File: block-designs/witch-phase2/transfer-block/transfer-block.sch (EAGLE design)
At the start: 15 parts, among them IC1 74LVC1G18DBVR, IC2 74AHC1G00DBV, IC3 741G3157DBVR, IC4 741G175, IC5 741G3157DBVR

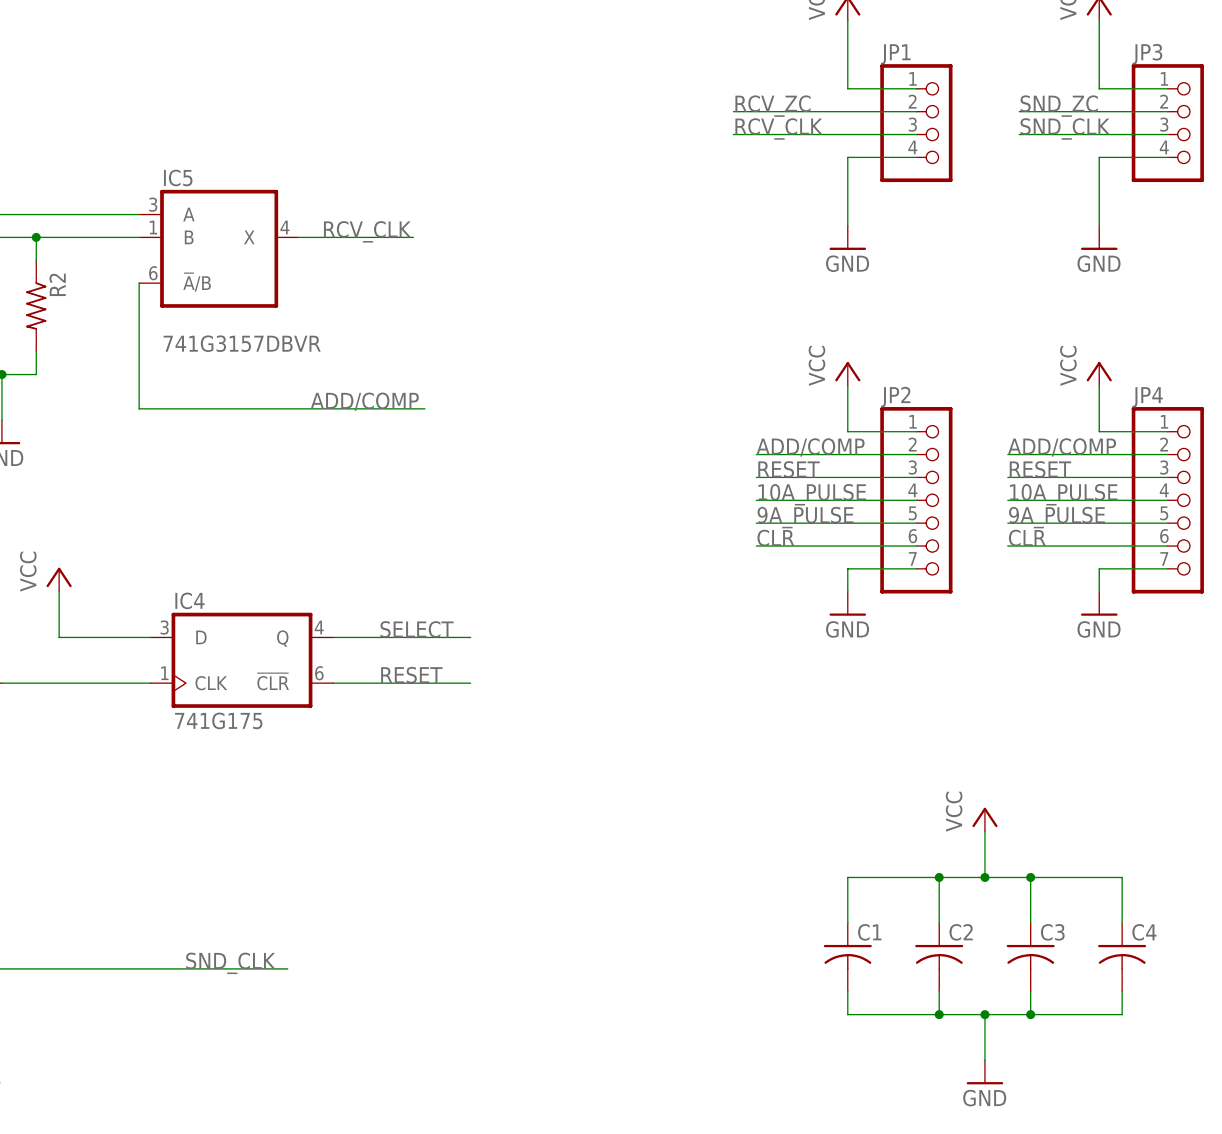
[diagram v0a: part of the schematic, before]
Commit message: updated designs for new labeling and spacing
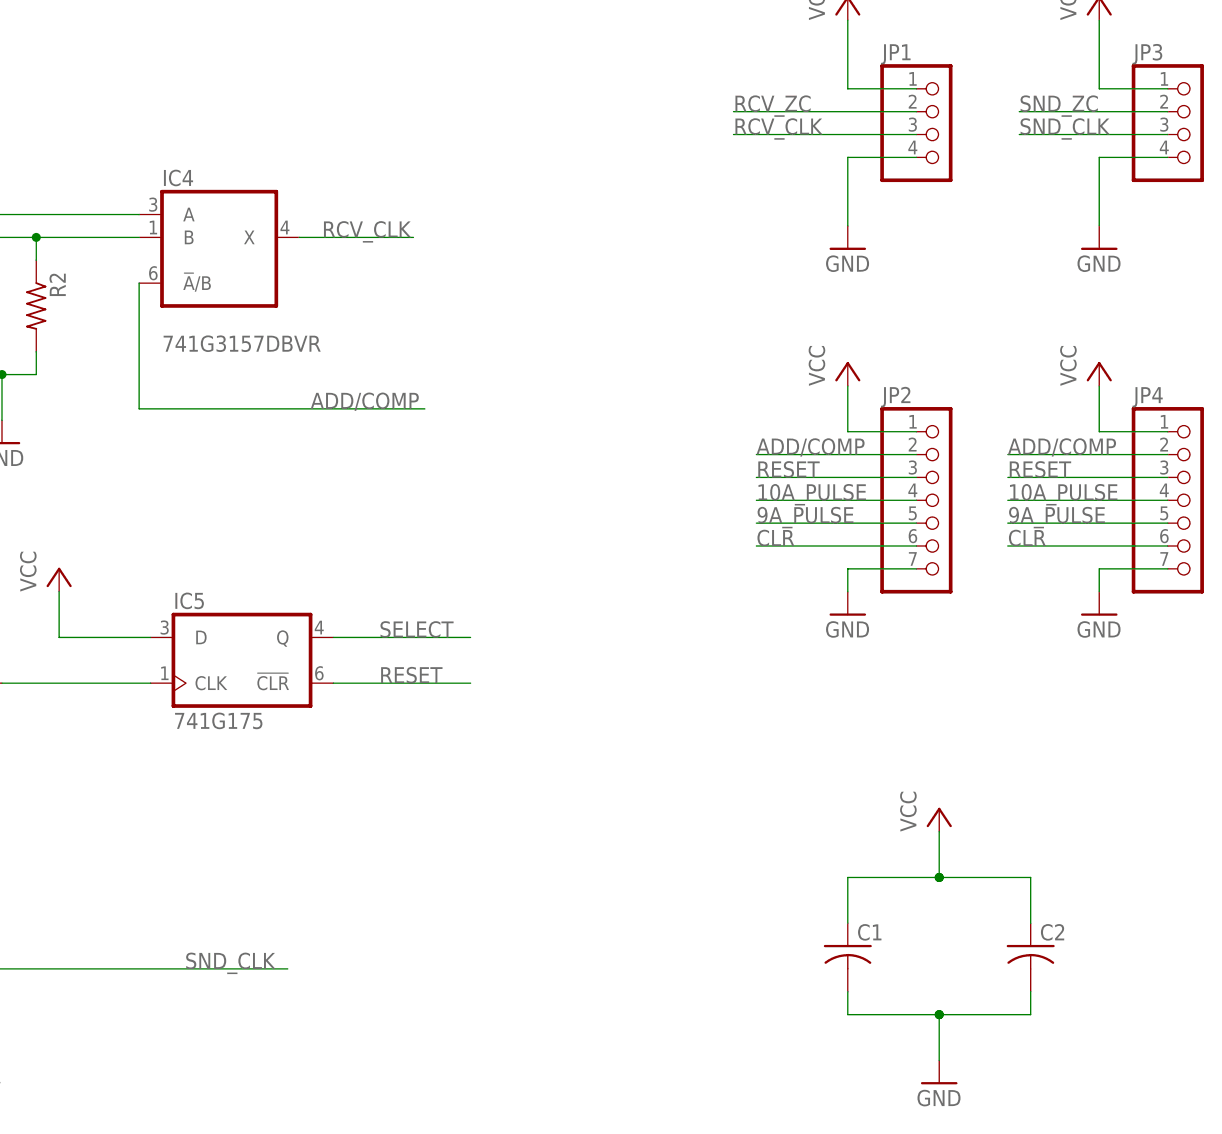
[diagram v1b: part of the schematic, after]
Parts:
- removed C3, C4: (no value), resistor:C-USC0805
- IC4: value 741G175 -> 741G3157DBVR; device 74xx-little-us:741G175 -> 74xx-little-us:741G3157DBVR
- IC5: value 741G3157DBVR -> 741G175; device 74xx-little-us:741G3157DBVR -> 74xx-little-us:741G175
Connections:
- net ADD/COMP: now also IC4G$1.!A!/B; no longer IC5G$1.!A!/B
- net GND: no longer C3.2, C4.2
- net N$4: now also IC4G$1.A; no longer IC5G$1.A
- net N$5: now also IC4G$1.B; no longer IC5G$1.B
- net RCV_CLK: now also IC4G$1.X; no longer IC5G$1.X
- net RESET: now also IC5G$1.!CLR; no longer IC4G$1.!CLR
- net SELECT: now also IC5G$1.Q; no longer IC4G$1.Q
- net VCC: now also IC5G$1.D; no longer C3.1, C4.1, IC4G$1.D
- net ZC_EN: now also IC5G$1.CLK; no longer IC4G$1.CLK
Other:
- moved on the sheet: C2
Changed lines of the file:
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@@
 <setting verticaltext="up"/>
 </settings>
-<grid distance="0.05" unitdist="inch" unit="inch" style="dots" multiple="1" display="no" altdistance="0.01" altunitdist="inch" altunit="inch"/>
+<grid distance="0.1" unitdist="inch" unit="inch" style="dots" multiple="1" display="no" altdistance="0.01" altunitdist="inch" altunit="inch"/>
 <layers>
 <layer number="1" name="Top" color="4" fill="1" visible="no" active="no"/>
@@
 <part name="GND5" library="supply1" deviceset="GND" device=""/>
 <part name="C1" library="resistor" deviceset="C-US" device="C0805"/>
+<part name="GND4" library="supply1" deviceset="GND" device=""/>
 <part name="C2" library="resistor" deviceset="C-US" device="C0805"/>
-<part name="C3" library="resistor" deviceset="C-US" device="C0805"/>
-<part name="GND4" library="supply1" deviceset="GND" device=""/>
-<part name="C4" library="resistor" deviceset="C-US" device="C0805"/>
 <part name="FRAME1" library="frames" deviceset="LETTER_L" device=""/>
 <part name="JP1" library="pinhead" deviceset="PINHD-1X4" device=""/>
@@
 <part name="JP4" library="pinhead" deviceset="PINHD-1X7" device=""/>
 <part name="IC1" library="74xx-little-us" deviceset="74*1G18" device="" value="74LVC1G18DBVR"/>
-<part name="IC5" library="74xx-little-us" deviceset="74*1G3157" device="DBVR"/>
+<part name="IC4" library="74xx-little-us" deviceset="74*1G3157" device="DBVR"/>
 <part name="P+4" library="supply1" deviceset="VCC" device=""/>
 <part name="P+2" library="supply1" deviceset="VCC" device=""/>
@@
 <part name="P+3" library="supply1" deviceset="VCC" device=""/>
 <part name="IC3" library="74xx-little-us" deviceset="74*1G3157" device="DBVR"/>
-<part name="IC4" library="74xx-little-us" deviceset="74*1G175" device=""/>
+<part name="IC5" library="74xx-little-us" deviceset="74*1G175" device=""/>
 </parts>
 <sheets>
@@
 <instance part="GND5" gate="1" x="207.01" y="148.59"/>
 <instance part="C1" gate="G$1" x="179.07" y="71.12"/>
-<instance part="C2" gate="G$1" x="189.23" y="71.12"/>
-<instance part="C3" gate="G$1" x="199.39" y="71.12"/>
-<instance part="GND4" gate="1" x="194.31" y="55.88"/>
-<instance part="C4" gate="G$1" x="209.55" y="71.12"/>
+<instance part="GND4" gate="1" x="189.23" y="55.88"/>
+<instance part="C2" gate="G$1" x="199.39" y="71.12"/>
 <instance part="FRAME1" gate="G$1" x="0" y="0"/>
 <instance part="FRAME1" gate="G$2" x="147.32" y="0"/>
@@
 <instance part="JP4" gate="A" x="217.17" y="120.65"/>
 <instance part="IC1" gate="G$1" x="60.96" y="148.59" rot="MR0"/>
-<instance part="IC5" gate="G$1" x="107.95" y="147.32"/>
-<instance part="P+4" gate="VCC" x="194.31" y="86.36"/>
+<instance part="IC4" gate="G$1" x="107.95" y="147.32"/>
+<instance part="P+4" gate="VCC" x="189.23" y="86.36"/>
 <instance part="P+2" gate="VCC" x="179.07" y="176.53"/>
 <instance part="P+5" gate="VCC" x="207.01" y="176.53"/>
@@
 <instance part="P+3" gate="VCC" x="179.07" y="135.89"/>
 <instance part="IC3" gate="G$1" x="72.39" y="66.04"/>
-<instance part="IC4" gate="G$1" x="109.22" y="102.87"/>
+<instance part="IC5" gate="G$1" x="109.22" y="102.87"/>
 </instances>
 <busses>
@@
 </segment>
 <segment>
-<pinref part="C3" gate="G$1" pin="2"/>
 <wire x1="179.07" y1="63.5" x2="189.23" y2="63.5" width="0.1524" layer="91"/>
-<wire x1="189.23" y1="63.5" x2="194.31" y2="63.5" width="0.1524" layer="91"/>
-<wire x1="194.31" y1="63.5" x2="199.39" y2="63.5" width="0.1524" layer="91"/>
-<wire x1="199.39" y1="63.5" x2="199.39" y2="66.04" width="0.1524" layer="91"/>
 <pinref part="C1" gate="G$1" pin="2"/>
 <wire x1="179.07" y1="66.04" x2="179.07" y2="63.5" width="0.1524" layer="91"/>
 <pinref part="C2" gate="G$1" pin="2"/>
-<wire x1="189.23" y1="66.04" x2="189.23" y2="63.5" width="0.1524" layer="91"/>
-<pinref part="C4" gate="G$1" pin="2"/>
-<wire x1="209.55" y1="66.04" x2="209.55" y2="63.5" width="0.1524" layer="91"/>
-<wire x1="209.55" y1="63.5" x2="199.39" y2="63.5" width="0.1524" layer="91"/>
-<junction x="199.39" y="63.5"/>
+<wire x1="199.39" y1="66.04" x2="199.39" y2="63.5" width="0.1524" layer="91"/>
+<wire x1="199.39" y1="63.5" x2="189.23" y2="63.5" width="0.1524" layer="91"/>
 <junction x="189.23" y="63.5"/>
 <pinref part="GND4" gate="1" pin="GND"/>
-<wire x1="194.31" y1="58.42" x2="194.31" y2="63.5" width="0.1524" layer="91"/>
-<junction x="194.31" y="63.5"/>
+<wire x1="189.23" y1="58.42" x2="189.23" y2="63.5" width="0.1524" layer="91"/>
+<junction x="189.23" y="63.5"/>
 </segment>
 <segment>
@@
 <segment>
 <pinref part="IC1" gate="G$1" pin="Y1"/>
-<pinref part="IC5" gate="G$1" pin="A"/>
+<pinref part="IC4" gate="G$1" pin="A"/>
 <wire x1="69.85" y1="152.4" x2="81.28" y2="152.4" width="0.1524" layer="91"/>
 <pinref part="R1" gate="G$1" pin="1"/>
@@
 <segment>
 <pinref part="IC1" gate="G$1" pin="Y0"/>
-<pinref part="IC5" gate="G$1" pin="B"/>
+<pinref part="IC4" gate="G$1" pin="B"/>
 <wire x1="69.85" y1="149.86" x2="88.9" y2="149.86" width="0.1524" layer="91"/>
 <pinref part="R2" gate="G$1" pin="1"/>
@@
 <net name="VCC" class="0">
 <segment>
-<pinref part="C3" gate="G$1" pin="1"/>
 <wire x1="179.07" y1="78.74" x2="189.23" y2="78.74" width="0.1524" layer="91"/>
-<wire x1="189.23" y1="78.74" x2="194.31" y2="78.74" width="0.1524" layer="91"/>
-<wire x1="194.31" y1="78.74" x2="199.39" y2="78.74" width="0.1524" layer="91"/>
-<wire x1="199.39" y1="78.74" x2="199.39" y2="73.66" width="0.1524" layer="91"/>
 <pinref part="C1" gate="G$1" pin="1"/>
 <wire x1="179.07" y1="73.66" x2="179.07" y2="78.74" width="0.1524" layer="91"/>
 <pinref part="C2" gate="G$1" pin="1"/>
-<wire x1="189.23" y1="73.66" x2="189.23" y2="78.74" width="0.1524" layer="91"/>
-<pinref part="C4" gate="G$1" pin="1"/>
-<wire x1="199.39" y1="78.74" x2="209.55" y2="78.74" width="0.1524" layer="91"/>
-<wire x1="209.55" y1="78.74" x2="209.55" y2="73.66" width="0.1524" layer="91"/>
+<wire x1="189.23" y1="78.74" x2="199.39" y2="78.74" width="0.1524" layer="91"/>
+<wire x1="199.39" y1="78.74" x2="199.39" y2="73.66" width="0.1524" layer="91"/>
 <junction x="189.23" y="78.74"/>
-<junction x="199.39" y="78.74"/>
-<wire x1="194.31" y1="78.74" x2="194.31" y2="83.82" width="0.1524" layer="91"/>
-<junction x="194.31" y="78.74"/>
+<wire x1="189.23" y1="78.74" x2="189.23" y2="83.82" width="0.1524" layer="91"/>
+<junction x="189.23" y="78.74"/>
 <pinref part="P+4" gate="VCC" pin="VCC"/>
 </segment>
@@
 <wire x1="91.44" y1="105.41" x2="91.44" y2="110.49" width="0.1524" layer="91"/>
 <pinref part="P+1" gate="VCC" pin="VCC"/>
-<pinref part="IC4" gate="G$1" pin="D"/>
+<pinref part="IC5" gate="G$1" pin="D"/>
 </segment>
 <segment>
@@
 <net name="ADD/COMP" class="0">
 <segment>
-<pinref part="IC5" gate="G$1" pin="!A!/B"/>
+<pinref part="IC4" gate="G$1" pin="!A!/B"/>
 <wire x1="100.33" y1="144.78" x2="100.33" y2="130.81" width="0.1524" layer="91"/>
 <wire x1="100.33" y1="130.81" x2="132.08" y2="130.81" width="0.1524" layer="91"/>
@@
 </segment>
 <segment>
-<pinref part="IC4" gate="G$1" pin="Q"/>
+<pinref part="IC5" gate="G$1" pin="Q"/>
 <wire x1="121.92" y1="105.41" x2="137.16" y2="105.41" width="0.1524" layer="91"/>
 <label x="127" y="105.41" size="1.778" layer="95"/>
@@
 <pinref part="IC2" gate="A" pin="O"/>
 <wire x1="85.09" y1="100.33" x2="101.6" y2="100.33" width="0.1524" layer="91"/>
-<pinref part="IC4" gate="G$1" pin="CLK"/>
+<pinref part="IC5" gate="G$1" pin="CLK"/>
 </segment>
 </net>
@@
 </segment>
 <segment>
-<pinref part="IC5" gate="G$1" pin="X"/>
+<pinref part="IC4" gate="G$1" pin="X"/>
 <wire x1="118.11" y1="149.86" x2="130.81" y2="149.86" width="0.1524" layer="91"/>
 <label x="120.65" y="149.86" size="1.778" layer="95"/>
@@
 </segment>
 <segment>
-<pinref part="IC4" gate="G$1" pin="!CLR"/>
+<pinref part="IC5" gate="G$1" pin="!CLR"/>
 <wire x1="121.92" y1="100.33" x2="137.16" y2="100.33" width="0.1524" layer="91"/>
 <label x="127" y="100.33" size="1.778" layer="95"/>

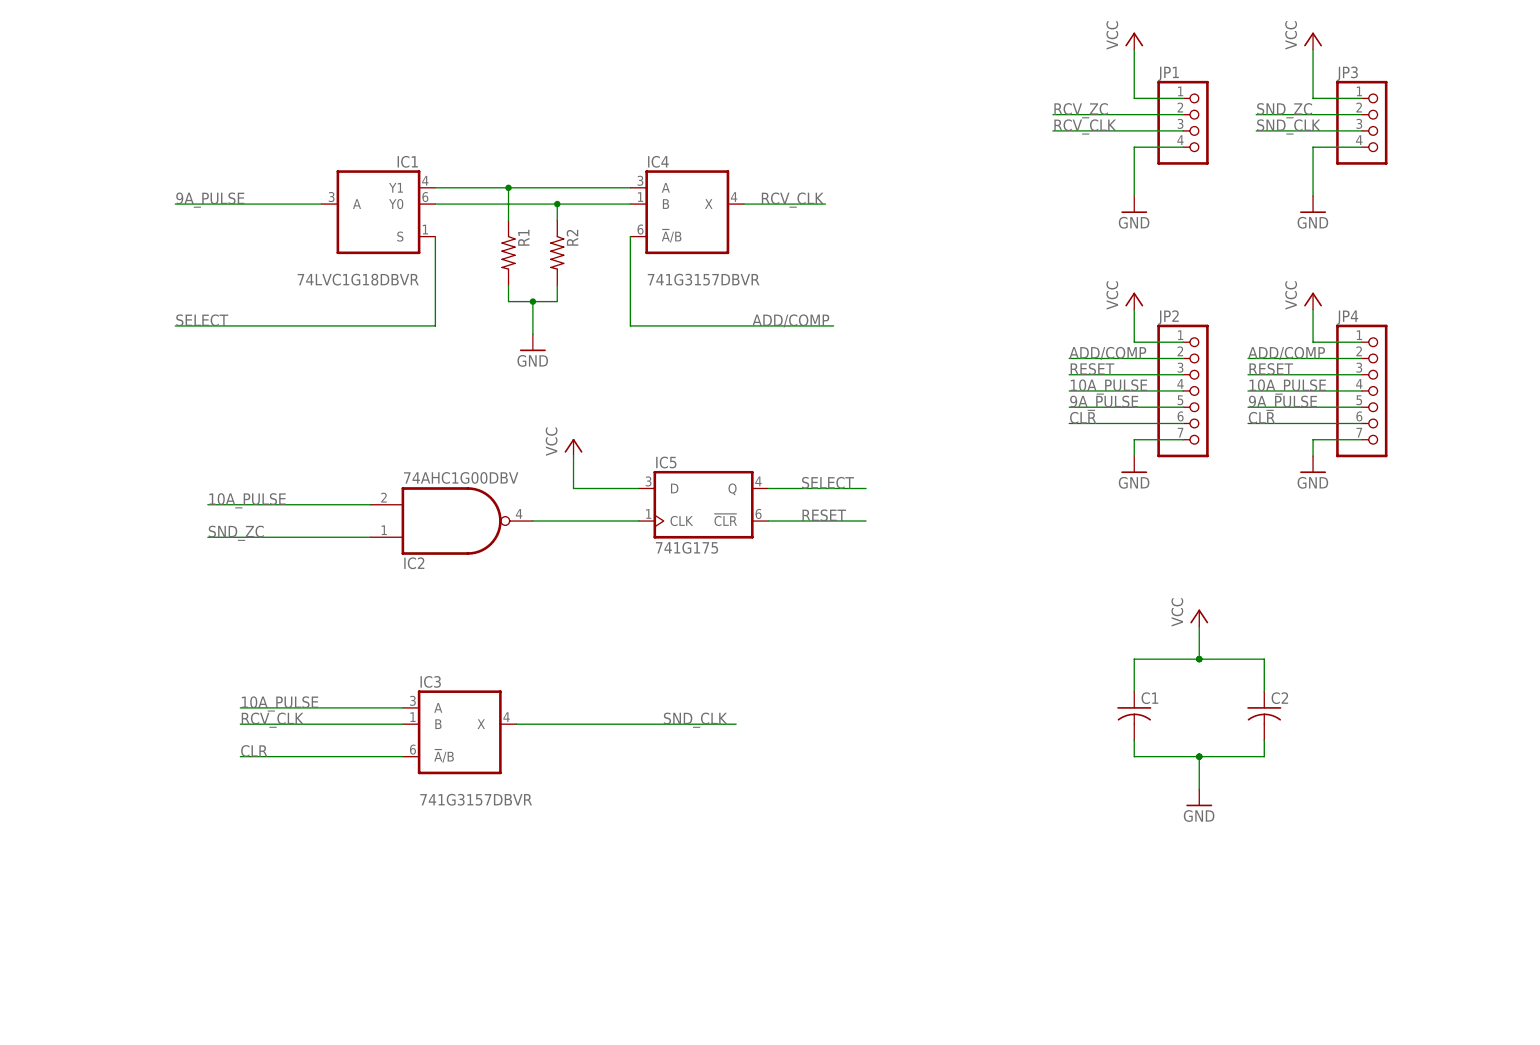
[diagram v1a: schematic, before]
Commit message: updated layout with additional caps and change to 0603 passive. changed clock input to use a 71LVC1G97 configured as AND gate with one input inverted
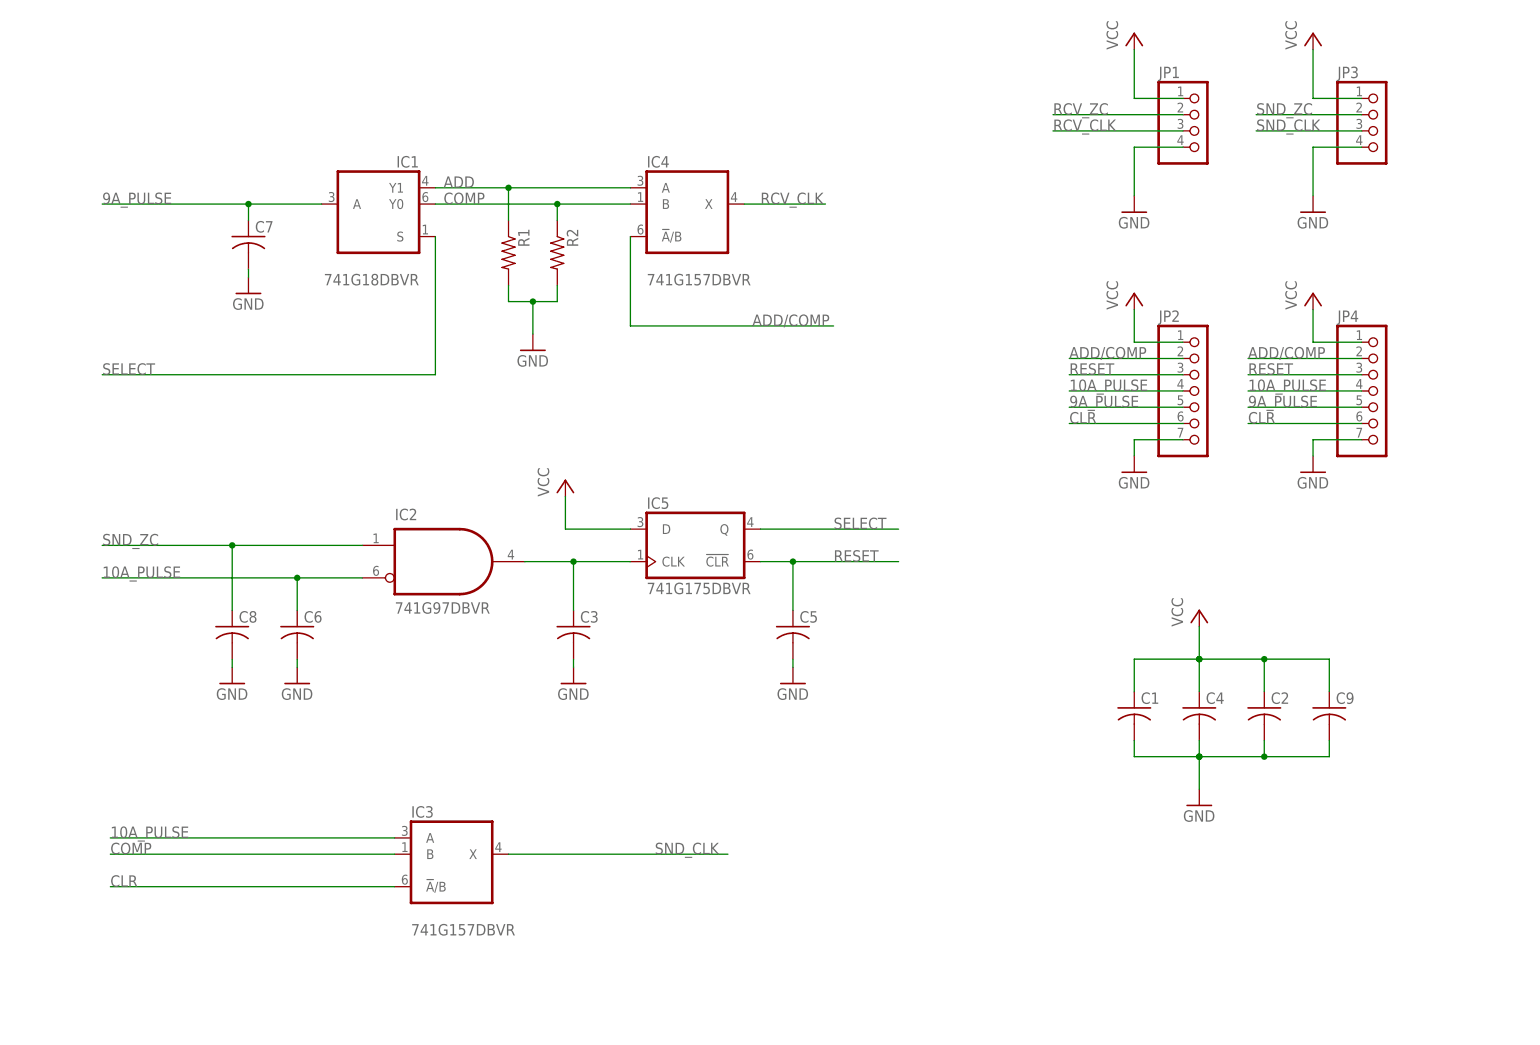
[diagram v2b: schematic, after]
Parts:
- added C3, C4, C5, C6, C7, C8, C9: (no value), resistor:C-USC0603K
- C1, C2: device resistor:C-USC0805 -> resistor:C-USC0603K
- IC1: value 74LVC1G18DBVR -> 741G18DBVR; device 74xx-little-us:741G18 -> witch-e:741G18
- IC2: value 74AHC1G00DBV -> 741G97DBVR; device 74xx-little-us:74AHC1G00DBV -> witch-e:741G97-AND-1INV
- IC3, IC4: value 741G3157DBVR -> 741G157DBVR
- IC5: value 741G175 -> 741G175DBVR; device 74xx-little-us:741G175 -> witch-e:741G175
- R1, R2: device resistor:R-US_R0805 -> resistor:R-US_R0603
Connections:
- net N$4 renamed ADD
- removed net N$5: IC1G$1.Y0, IC4G$1.B, R2.1
- new net COMP: IC1G$1.Y0, IC3G$1.B, IC4G$1.B, R2.1
- net 10A_PULSE: now also C6.1, IC2G$1.I0; no longer IC2A.I1
- net 9A_PULSE: now also C7.1
- net GND: now also C3.2, C4.2, C5.2, C6.2, C7.2, C8.2, C9.2
- net RCV_CLK: no longer IC3G$1.B
- net RESET: now also C5.1
- net SND_ZC: now also C8.1, IC2G$1.I1; no longer IC2A.I0
- net VCC: now also C4.1, C9.1
- net ZC_EN: now also C3.1, IC2G$1.O; no longer IC2A.O
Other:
- moved on the sheet: IC3, IC5
